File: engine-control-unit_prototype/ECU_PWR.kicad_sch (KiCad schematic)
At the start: 27 parts

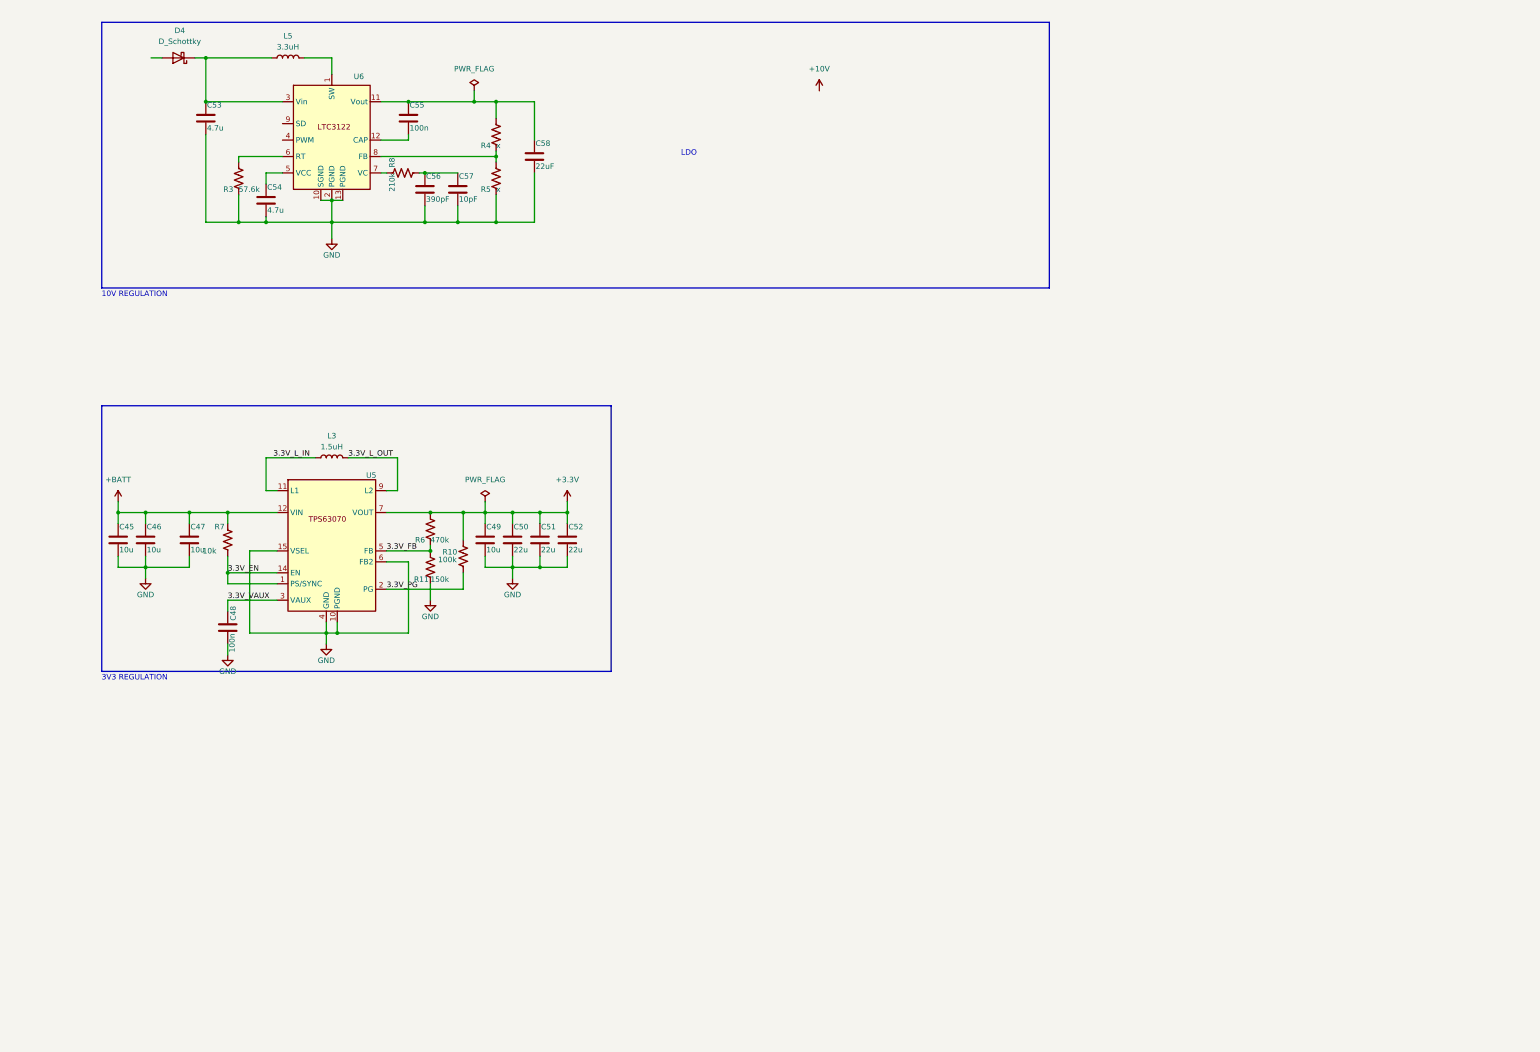
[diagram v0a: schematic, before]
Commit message: Added power circuitry without components values
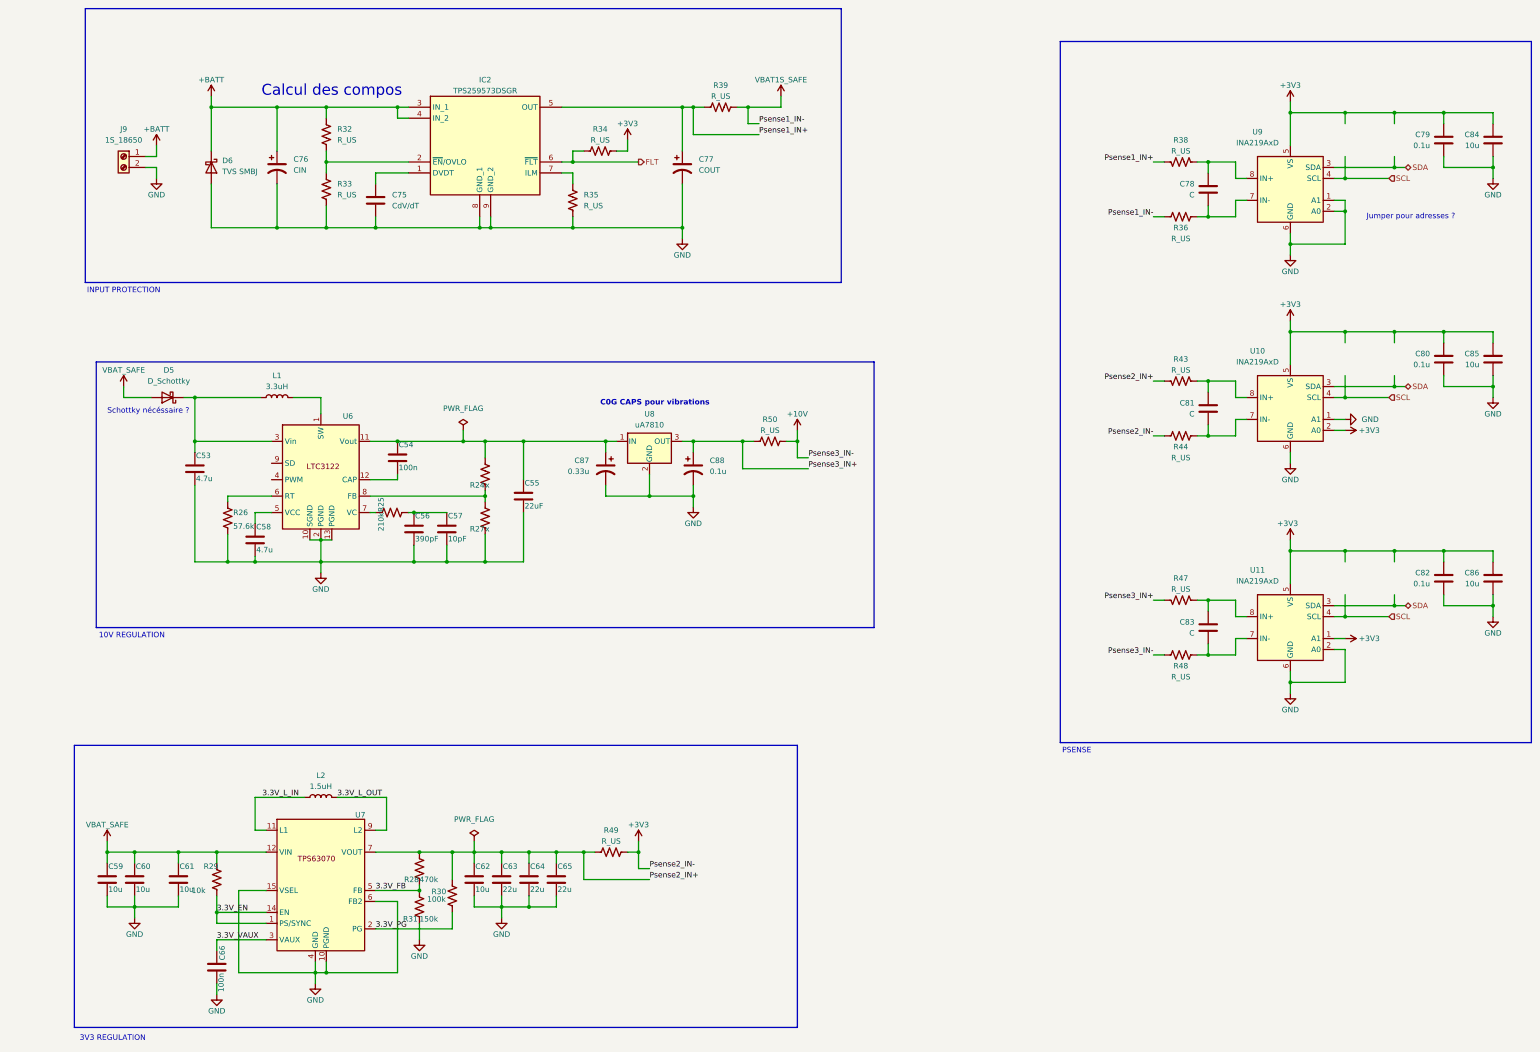
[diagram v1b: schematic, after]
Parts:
- added C75: CdV/dT, symbol Device:C
- added C76: CIN, symbol Device:C_Polarized_US
- added C77: COUT, symbol Device:C_Polarized_US
- added C78, C81, C83: C, symbol Device:C
- added C79, C80, C82: 0.1u, symbol Device:C
- added C84, C85, C86: 10u, symbol Device:C
- added C87: 0.33u, symbol Device:C_Polarized_US
- added C88: 0.1u, symbol Device:C_Polarized_US
- added D6: TVS SMBJ, symbol Device:D_Schottky
- added IC2: TPS259573DSGR, SON50P200X200X80-9N, symbol TPS259573DSGR:TPS259573DSGR
- added J9: 1S_18650, symbol Connector:Screw_Terminal_01x02
- added R32, R33, R34, R35, R36, R38, R39, R43, R44, R47, R48, R49, R50: R_US, symbol Device:R_US
- added U10, U11, U9: INA219AxD, Package_SO:SOIC-8_3.9x4.9mm_P1.27mm, symbol Sensor_Energy:INA219AxD
- added U8: uA7810, symbol Regulator_Linear:uA7810
- renumbered C55 to C54, C58 to C55, C54 to C58, C45 to C59, C46 to C60, C47 to C61, C49 to C62, C50 to C63, C51 to C64, C52 to C65, C48 to C66, D4 to D5, L5 to L1, L3 to L2, R4 to R24, R8 to R25, R3 to R26, R5 to R27, R6 to R28, R7 to R29, R10 to R30, R11 to R31, U5 to U7
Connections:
- net +10V: now also R48.2, R50.2
- net +BATT: now also C76.1, D6.1 (K), IC2.3 (IN_1), IC2.4 (IN_2), J9.1 (Pin_1), R32.1; no longer C59.1, C60.1, C61.1, R29.1, U7.12 (VIN), U7.13 (VIN)
- net GND: now also C75.2, C76.2, C77.2, C79.1, C80.1, C82.1, C84.1, C85.1, C86.1, C87.2, C88.2, D6.2 (A), IC2.8 (GND_1), IC2.9 (GND_2), J9.2 (Pin_2), R33.2, R35.2, U10.1 (A1), U10.6 (GND), U11.2 (A0), U11.6 (GND), U8.2 (GND), U9.1 (A1), U9.2 (A0), U9.6 (GND)
- net at C54.1, C55.1, R24.1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: now also C87.1, U8.1 (IN)
- net VBAT_SAFE: now reaches D5.2 (A)
- net VBAT_SAFE: now also C59.1, C60.1, C61.1, R29.1, U7.12 (VIN), U7.13 (VIN)
- net +3.3V renamed Psense2_IN+
- net Psense2_IN+: now also R43.2, R49.1
- new net: C78.1, R36.1, U9.7 (IN-)
- new net: C78.2, R38.1, U9.8 (IN+)
- new net: C83.2, R47.1, U11.8 (IN+)
- new net: IC2.7 (ILM), R35.1
- new net: C83.1, R48.1, U11.7 (IN-)
- new net: C75.1, IC2.1 (DVDT)
- new net: IC2.2 (~{EN}/OVLO), R32.2, R33.1
- new net: C81.1, R44.1, U10.7 (IN-)
- new net: C81.2, R43.1, U10.8 (IN+)
- new net +3V3: C79.2, C80.2, C82.2, C84.2, C85.2, C86.2, R34.2, R44.2, R49.2, U10.2 (A0), U10.5 (VS), U11.1 (A1), U11.5 (VS), U9.5 (VS)
- new net FLT: IC2.6 (~{FLT}), R34.1
- new net Psense1_IN+: C77.1, IC2.5 (OUT), R38.2, R39.1
- new net Psense3_IN+: C88.1, R47.2, R50.1, U8.3 (OUT)
- new net SCL: U10.4 (SCL), U11.4 (SCL), U9.4 (SCL)
- new net SDA: U10.3 (SDA), U11.3 (SDA), U9.3 (SDA)
- new net VBAT1S_SAFE: R36.2, R39.2
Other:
- note added: "C0G CAPS pour vibrations"
- note added: "Calcul des compos"
- note added: "INPUT PROTECTION"
- note added: "Jumper pour adresses ?"
- note added: "PSENSE"
- note added: "Schottky nécéssaire ?"
- note removed: "LDO"
- moved on the sheet: C53, C54, C55, C56, C57, C58, C59, C60, C61, C62, C63, C64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

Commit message: Modified SD card Fixed INA826 decoupling caps Removed reset button Added Ports connectors (headers for ease of access)
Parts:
- removed C85, C86: 10u, symbol Device:C
- removed C87: 0.33u, symbol Device:C_Polarized_US
- removed C88: 0.1u, symbol Device:C_Polarized_US
- removed U8: uA7810, symbol Regulator_Linear:uA7810
- added TP1: IN1+, symbol Connector:TestPoint
- added TP2: IN1-, symbol Connector:TestPoint
- added TP3: IN2+, symbol Connector:TestPoint
- added TP4: IN2-, symbol Connector:TestPoint
- added TP5: IN3+, symbol Connector:TestPoint
- added TP6: IN3-, symbol Connector:TestPoint
- added U12: LT3042xMSE, Package_SO:MSOP-10-1EP_3x3mm_P0.5mm_EP1.68x1.88mm, symbol Regulator_Linear:LT3042xMSE
- J9: value 1S_18650 -> 1-2S_18650
- R24, R27: value x -> TBD
- R26: value 57.6k -> 57k6
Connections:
- net VBAT1S_SAFE is gone; now on net VBAT_SAFE: R36.2, R39.2
- net +10V: now also TP6.1
- net +3V3: now also TP4.1
- net Psense1_IN+: now also TP1.1
- net Psense2_IN+: now also TP3.1
- net Psense3_IN+: now also TP5.1
- net VBAT_SAFE: now also TP2.1
- new net: U12.1 (IN), U12.2 (IN)
- new net: U12.11 (GND), U12.8 (GND)
- no-connect marks 0 -> 2
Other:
- note removed: "C0G CAPS pour vibrations"
- moved on the sheet: C54, C55, C56, C57, C59, C60, C61, C62, C63, C64, C65, C79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

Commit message: Removed bloat libraries Changed symbols for Sirius custom library Changed layout for one page
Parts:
- removed C53, C58: 4.7u, 0CSL_D1_V1:C0805_MAN, symbol Device:C
- removed C54, C66: 100n, 0CSL_D1_V1:C0603_MAN, symbol Device:C
- removed C55: 22uF, 0CSL_D1_V1:C0805_MAN, symbol Device:C
- removed C56: 390pF, 0CSL_D1_V1:C0805_MAN, symbol Device:C
- removed C57: 10pF, 0CSL_D1_V1:C0805_MAN, symbol Device:C
- removed C59, C60: 10u, 0CSL_D1_V1:C0805_MAN, symbol Device:C
- removed C61, C62: 10u, 0CSL_D1_V1:C0603_MAN, symbol Device:C
- removed C63, C64, C65: 22u, 0CSL_D1_V1:C0805_MAN, symbol Device:C
- removed D5: D_Schottky, symbol Device:D_Schottky
- removed L1: 3.3uH, 0CSL_D1_V1:CUSTOM_BMRA000606301R5MA1, symbol Device:L
- removed L2: 1.5uH, 0CSL_D1_V1:CUSTOM_BMRA000606301R5MA1, symbol Device:L
- removed R24, R27: TBD, 0CSL_D1_V1:R0603_MAN, symbol Device:R_US
- removed R25: 210k, 0CSL_D1_V1:R0603_MAN, symbol Device:R_US
- removed R26: 57k6, 0CSL_D1_V1:R0603_MAN, symbol Device:R_US
- removed R28: 470k, 0CSL_D1_V1:R0603_MAN, symbol Device:R_US
- removed R29: 10k, 0CSL_D1_V1:R0603_MAN, symbol Device:R_US
- removed R30: 100k, 0CSL_D1_V1:R0603_MAN, symbol Device:R_US
- removed R31: 150k, 0CSL_D1_V1:R0603_MAN, symbol Device:R_US
- removed U6: ~, Footprint:MSOP-12_MSE, symbol 0CSL_D1_V1:LTC3122
- removed U7: ~, 0CSL_D1_V1:CUSTOM_VREG_TPS63070RNMR, symbol 0CSL_D1_V1:Custom_TPS63070
- J9: value 1-2S_18650 -> 2S_18650
- R39, R49, R50: value R_US -> 10m
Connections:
- net +BATT renamed +BATT1
- no-connect marks 2 -> 0
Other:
- note removed: "Schottky nécéssaire ?"
- moved on the sheet: U12
